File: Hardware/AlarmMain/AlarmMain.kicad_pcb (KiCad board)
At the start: 4 copper layers, 244 x 109 mm, 220 parts, among them J1 debugWIRE, J10 I2C, J11 ICSP, J12 AUX, J13 RS485 1, J14 PWR, J15 BATT, J16 12V, J17 DI1, J18 DI2, J19 DI3, J2 OP1, J20 DI4, J21 DI5, J22 DI6, J23 DI7, J24 DI8, J25 RS485 2, J3 OP3, J4 DI9, J5 DI10, J6 OP2, J7 OP4, J8 DI11, J9 DI12, Q1 STP40NF03L, Q2 STP40NF03L, Q3 STP40NF03L, Q4 STP40NF03L, Q5 IRF9540N, Q6 IRF540N, Q7 BC337, SW1 RESET, U1 ATmega328P-PU, U10 LM317_TO-220, U11 LM324, U12 7805, U13 LM339, U14 LM339, U15 LM339, U16 LM339, U2 LM339, U3 LM339, U4 MCP23017_SP, U5 MAX483E, U6 MCP7940N-xSN, U7 STTS75, U8 STWD100, U9 MAX483E, Y1 20Mhz, Y2 32.768k

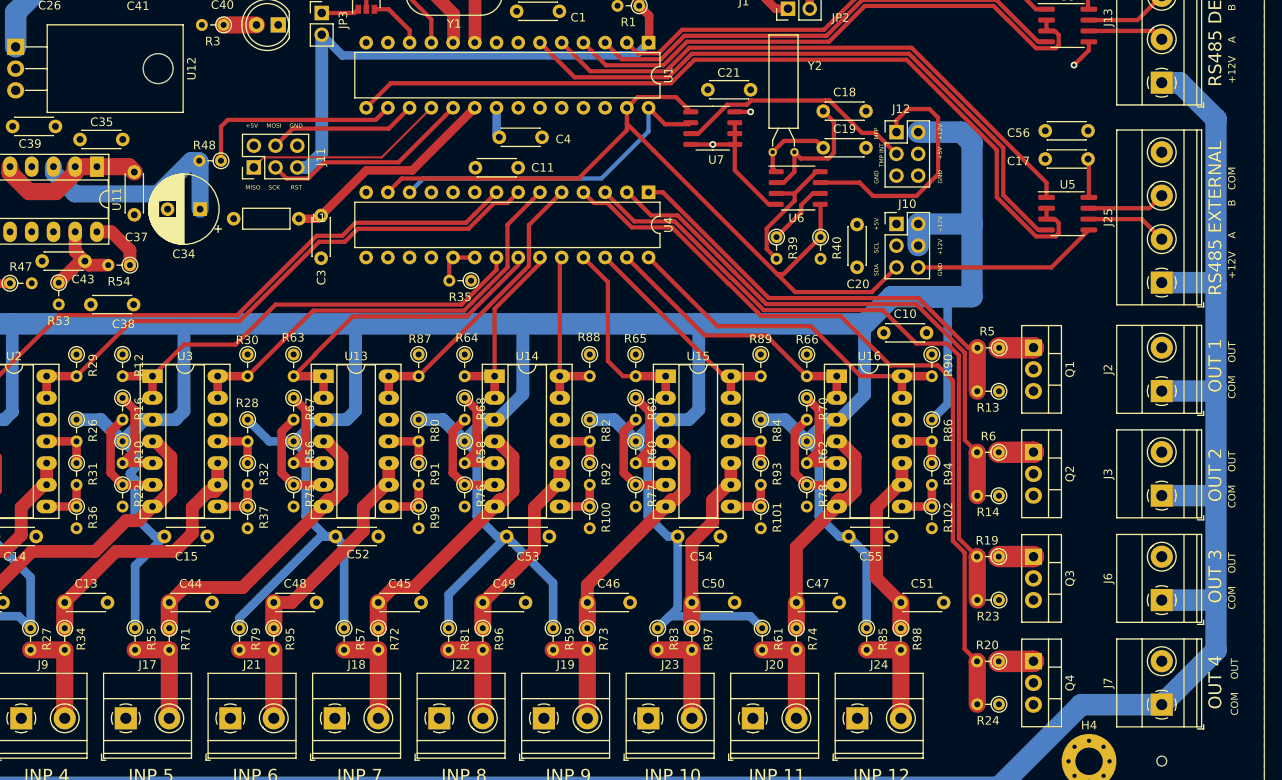
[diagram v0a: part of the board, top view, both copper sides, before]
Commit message: Rev 1.1 (Power boot zener)
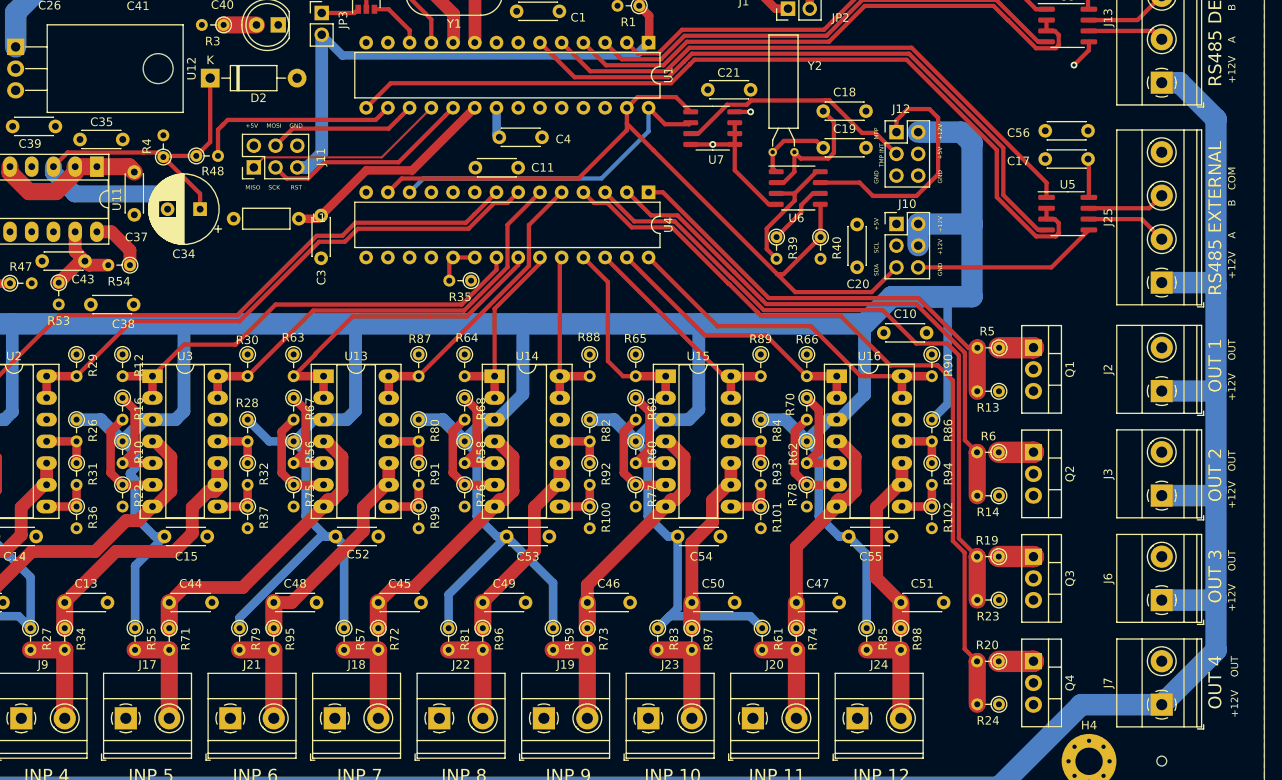
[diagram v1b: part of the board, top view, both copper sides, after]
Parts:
- added D2: 5V1, Diode_THT:D_DO-41_SOD81_P10.16mm_Horizontal, F.Cu at (108.7, 10.2)
- added R4: 100K, Resistor_THT:R_Axial_DIN0204_L3.6mm_D1.6mm_P2.54mm_Vertical, F.Cu at (103.3, 19.4)
- moved R48 2.94 mm to (107.1, 19.2), turned to 0 degrees
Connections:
- R48 pad 1: VBAT_PWM -> Net-(C34-Pad1)
- R48 pad 2: Net-(C34-Pad1) -> VBAT_PWM
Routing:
- net Net-(C34-Pad1): track 26.1 -> 49.2 mm
- net VIN: track 149.3 -> 160.1 mm
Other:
- board text added: "+12V OUT"
- board text removed: "COM OUT"
